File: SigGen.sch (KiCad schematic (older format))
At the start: 4 parts, among them M1 HC-SR08-AD9851, U1 ILI9341_SPI_Touch_SD

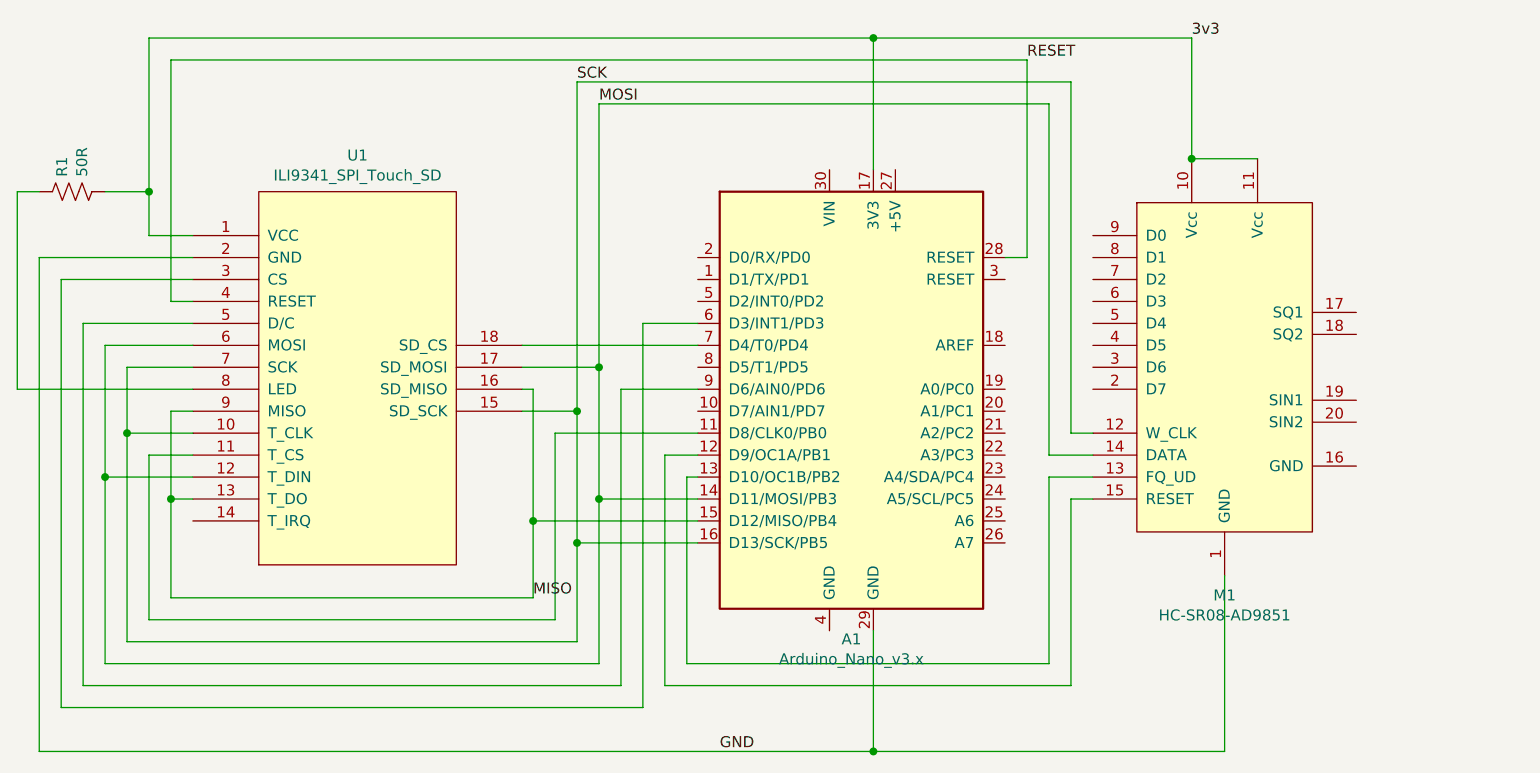
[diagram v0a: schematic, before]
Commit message: Added test points for external wiring
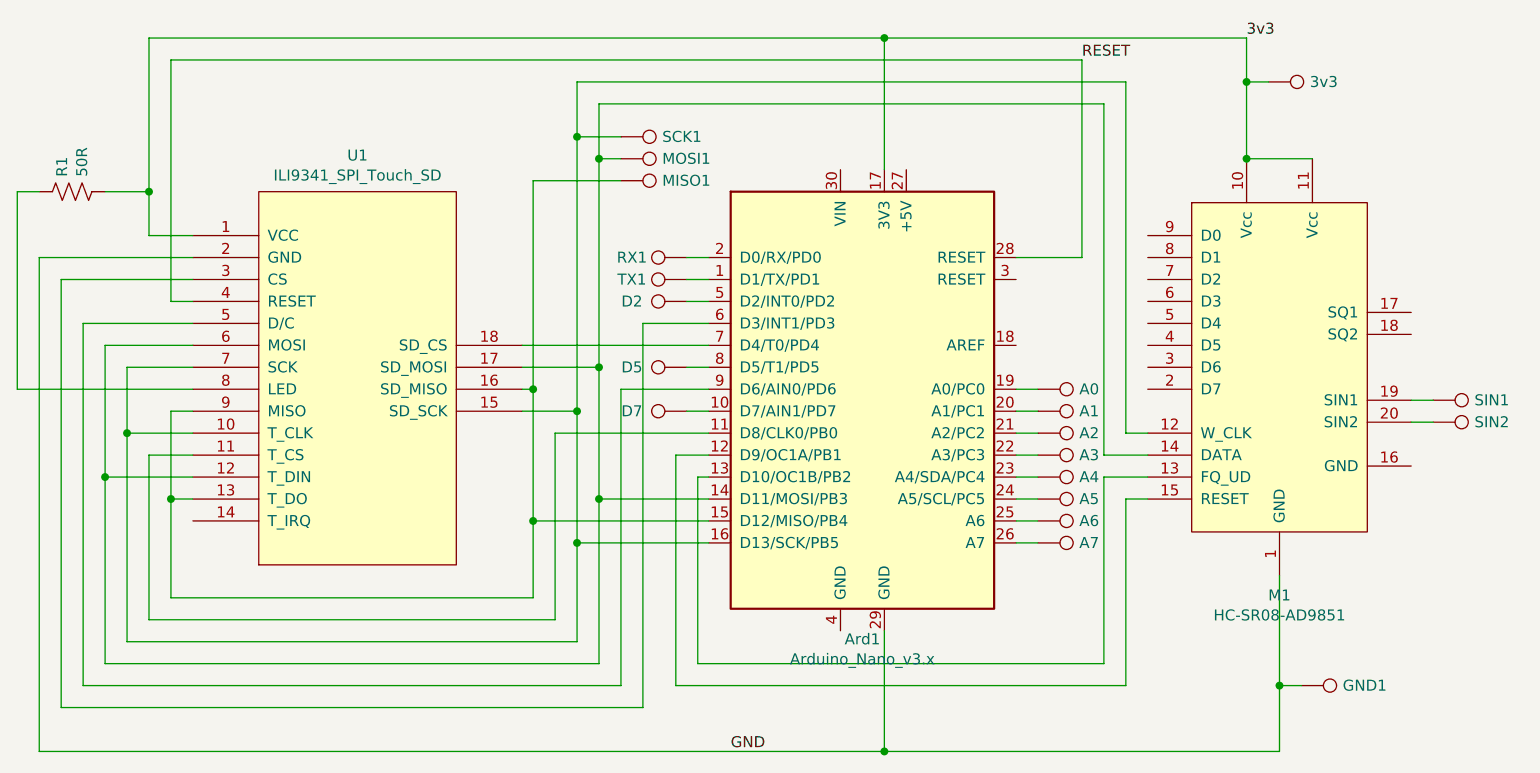
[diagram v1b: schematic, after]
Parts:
- added 3v3, A0, A1, A2, A3, A4, A5, A6, A7, D2, D5, D7, GND1, MISO1, MOSI1, RX1, SCK1, SIN1, SIN2, TX1: TestPoint, SigGen:Testpoint, symbol Connector:TestPoint
- renumbered A1 to Ard1
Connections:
- net 3v3: now also 3v3.1
- net GND: now also GND1.1
- net at Ard1.1 (D1/TX/PD1): now also TX1.1
- net at Ard1.10 (D7/AIN1/PD7): now also D7.1
- net at Ard1.19 (A0/PC0): now also A0.1
- net at Ard1.2 (D0/RX/PD0): now also RX1.1
- net at Ard1.20 (A1/PC1): now also A1.1
- net at Ard1.21 (A2/PC2): now also A2.1
- net at Ard1.22 (A3/PC3): now also A3.1
- net at Ard1.23 (A4/SDA/PC4): now also A4.1
- net at Ard1.24 (A5/SCL/PC5): now also A5.1
- net at Ard1.25 (A6): now also A6.1
- net at Ard1.26 (A7): now also A7.1
- net at Ard1.5 (D2/INT0/PD2): now also D2.1
- net at Ard1.8 (D5/T1/PD5): now also D5.1
- net at M1.19 (SIN1): now also SIN1.1
- net at M1.20 (SIN2): now also SIN2.1
- net MISO: no longer names the net of Ard1.15 (D12/MISO/PB4), U1.13 (T_DO), U1.16 (SD_MISO), U1.9 (MISO)
- net MISO: now also MISO1.1
- net MOSI: no longer names the net of Ard1.14 (D11/MOSI/PB3), M1.14 (DATA), U1.12 (T_DIN), U1.17 (SD_MOSI), U1.6 (MOSI)
- net MOSI: now also MOSI1.1
- net SCK: no longer names the net of Ard1.16 (D13/SCK/PB5), M1.12 (W_CLK), U1.10 (T_CLK), U1.15 (SD_SCK), U1.7 (SCK)
- net SCK: now also SCK1.1
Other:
- moved on the sheet: Ard1, M1
